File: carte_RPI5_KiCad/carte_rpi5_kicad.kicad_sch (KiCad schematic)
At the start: 30 parts, among them J1 Conn_01x03, J10 RPI5_40pins, J2 Conn_01x03, J3 Conn_01x03, J4 Conn_01x03, J5 Conn_01x03, J6 Conn_01x03, J7 Conn_01x03, J8 Conn_01x03, J9 XT60-M, SW1 SW_SPDT

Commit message: Mise à jour du PCB
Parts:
- F1: footprint Fuse:Fuse_0402_1005Metric -> librairie_empreintes:PTF-50
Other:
- note removed: "Demander à Thomas résistance sur interrupteur"
- note removed: "Rajouter des pins pour le moteur ; demander à Thomas pour les empreintes des pins"
- moved on the sheet: Conn_LPS22HB1, J10, R_SCL2, R_SDA2

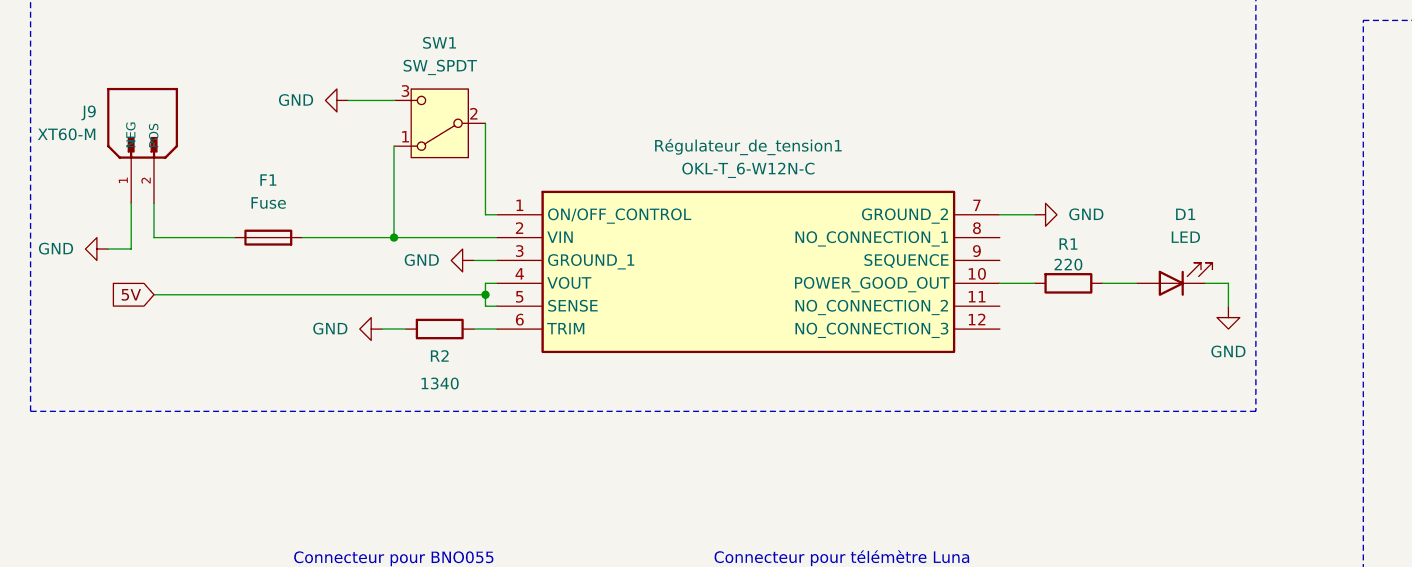
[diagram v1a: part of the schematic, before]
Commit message: changement_sens_connecteur_RPI
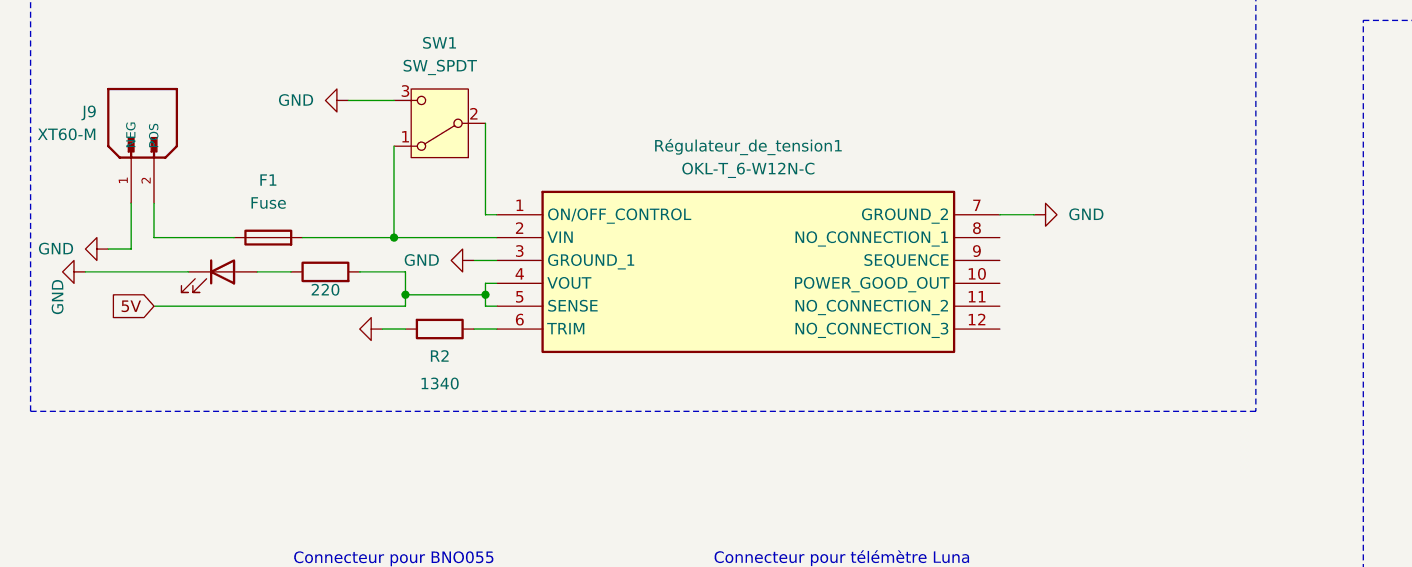
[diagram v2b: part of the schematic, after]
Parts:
- R1, R2, R_SCL2, R_SDA2: footprint Resistor_SMD:R_0805_2012Metric -> Resistor_SMD:R_1206_3216Metric_Pad1.30x1.75mm_HandSolder
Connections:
- net 5V: now also R1.2
- net at Régulateur_de_tension1.10 (POWER_GOOD_OUT): no longer R1.2
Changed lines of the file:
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@@
 	)
 	(junction
-		(at 66.04 49.53)
-		(diameter 0)
-		(color 0 0 0 0)
-	)
-	(junction
 		(at 345.44 218.44)
 		(diameter 0)
@@
 	)
 	(junction
+		(at 57.15 49.53)
+		(diameter 0)
+		(color 0 0 0 0)
+	)
+	(junction
 		(at 165.1 125.73)
 		(diameter 0)
@@
 	)
 	(junction
+		(at 66.04 49.53)
+		(diameter 0)
+		(color 0 0 0 0)
+	)
+	(junction
 		(at 247.65 39.37)
 		(diameter 0)
@@
 	(wire
 		(pts
+			(xy 66.04 49.53) (xy 66.04 50.8)
+		)
+		(stroke
+			(width 0)
+			(type default)
+		)
+	)
+	(wire
+		(pts
 			(xy 165.1 109.22) (xy 165.1 114.3)
 		)
@@
 	(wire
 		(pts
+			(xy 29.21 50.8) (xy 57.15 50.8)
+		)
+		(stroke
+			(width 0)
+			(type default)
+		)
+	)
+	(wire
+		(pts
 			(xy 66.04 48.26) (xy 66.04 49.53)
 		)
@@
 	(wire
 		(pts
-			(xy 123.19 48.26) (xy 127 48.26)
-		)
-		(stroke
-			(width 0)
-			(type default)
-		)
-	)
-	(wire
-		(pts
 			(xy 242.57 53.34) (xy 247.65 53.34)
 		)
@@
 	(wire
 		(pts
-			(xy 134.62 48.26) (xy 138.43 48.26)
-		)
-		(stroke
-			(width 0)
-			(type default)
-		)
-	)
-	(wire
-		(pts
 			(xy 63.5 156.21) (xy 63.5 161.29)
 		)
@@
 	(wire
 		(pts
-			(xy 148.59 48.26) (xy 148.59 50.8)
+			(xy 57.15 46.99) (xy 57.15 49.53)
 		)
 		(stroke
@@
 	(wire
 		(pts
-			(xy 198.12 143.51) (xy 205.74 143.51)
+			(xy 44.45 46.99) (xy 40.64 46.99)
 		)
 		(stroke
@@
 	(wire
 		(pts
-			(xy 186.69 72.39) (xy 186.69 73.66)
+			(xy 198.12 143.51) (xy 205.74 143.51)
 		)
 		(stroke
@@
 	(wire
 		(pts
-			(xy 176.53 151.13) (xy 185.42 151.13)
+			(xy 186.69 72.39) (xy 186.69 73.66)
 		)
 		(stroke
@@
 	(wire
 		(pts
-			(xy 203.2 120.65) (xy 205.74 120.65)
+			(xy 176.53 151.13) (xy 185.42 151.13)
 		)
 		(stroke
@@
 	(wire
 		(pts
-			(xy 55.88 43.18) (xy 67.31 43.18)
+			(xy 57.15 49.53) (xy 57.15 50.8)
 		)
 		(stroke
@@
 	(wire
 		(pts
-			(xy 55.88 33.02) (xy 55.88 43.18)
+			(xy 203.2 120.65) (xy 205.74 120.65)
 		)
 		(stroke
@@
 	(wire
 		(pts
-			(xy 146.05 48.26) (xy 148.59 48.26)
+			(xy 55.88 43.18) (xy 67.31 43.18)
 		)
 		(stroke
@@
 	(wire
 		(pts
-			(xy 29.21 49.53) (xy 66.04 49.53)
+			(xy 55.88 33.02) (xy 55.88 43.18)
 		)
 		(stroke
@@
 	(wire
 		(pts
+			(xy 33.02 46.99) (xy 21.59 46.99)
+		)
+		(stroke
+			(width 0)
+			(type default)
+		)
+	)
+	(wire
+		(pts
 			(xy 317.5 227.33) (xy 349.25 227.33)
 		)
@@
 	(wire
 		(pts
+			(xy 52.07 46.99) (xy 57.15 46.99)
+		)
+		(stroke
+			(width 0)
+			(type default)
+		)
+	)
+	(wire
+		(pts
 			(xy 242.57 50.8) (xy 247.65 50.8)
 		)
@@
 	(wire
 		(pts
-			(xy 66.04 49.53) (xy 66.04 50.8)
+			(xy 198.12 125.73) (xy 205.74 125.73)
 		)
 		(stroke
@@
 	(wire
 		(pts
-			(xy 198.12 125.73) (xy 205.74 125.73)
+			(xy 57.15 49.53) (xy 66.04 49.53)
 		)
 		(stroke
@@
 	(global_label "5V"
 		(shape input)
-		(at 29.21 49.53 180)
+		(at 29.21 50.8 180)
 		(fields_autoplaced yes)
 		(effects
@@
 		)
 		(property "Intersheetrefs" "${INTERSHEET_REFS}"
-			(at 23.9267 49.53 0)
+			(at 23.9267 50.8 0)
 			(effects
 				(font
@@
 	(symbol
 		(lib_id "Device:LED")
-		(at 142.24 48.26 180)
+		(at 36.83 46.99 0)
 		(unit 1)
 		(exclude_from_sim no)
@@
 		(fields_autoplaced yes)
 		(property "Reference" "D1"
-			(at 143.8275 40.64 0)
+			(at 35.2425 54.61 0)
 			(effects
 				(font
 					(size 1.27 1.27)
 				)
+				(hide yes)
 			)
 		)
 		(property "Value" "LED"
-			(at 143.8275 43.18 0)
+			(at 35.2425 52.07 0)
 			(effects
 				(font
 					(size 1.27 1.27)
 				)
+				(hide yes)
 			)
 		)
 		(property "Footprint" "LED_SMD:LED_0805_2012Metric"
-			(at 142.24 48.26 0)
+			(at 36.83 46.99 0)
 			(effects
 				(font
@@
 		)
 		(property "Datasheet" "~"
-			(at 142.24 48.26 0)
+			(at 36.83 46.99 0)
 			(effects
 				(font
@@
 		)
 		(property "Description" "Light emitting diode"
-			(at 142.24 48.26 0)
+			(at 36.83 46.99 0)
 			(effects
 				(font
@@
 		)
 		(property "Sim.Pins" "1=K 2=A"
-			(at 142.24 48.26 0)
+			(at 36.83 46.99 0)
 			(effects
 				(font
@@
 			)
 		)
-		(property "Footprint" "Resistor_SMD:R_0805_2012Metric"
+		(property "Footprint" "Resistor_SMD:R_1206_3216Metric_Pad1.30x1.75mm_HandSolder"
 			(at 60.96 51.562 90)
 			(effects
@@
 			)
 		)
-		(property "Footprint" "Resistor_SMD:R_0805_2012Metric"
+		(property "Footprint" "Resistor_SMD:R_1206_3216Metric_Pad1.30x1.75mm_HandSolder"
 			(at 163.322 118.11 90)
 			(effects
@@
 	(symbol
 		(lib_id "Device:R")
-		(at 130.81 48.26 270)
+		(at 48.26 46.99 90)
 		(unit 1)
 		(exclude_from_sim no)
@@
 		(dnp no)
 		(property "Reference" "R1"
-			(at 130.81 43.942 90)
+			(at 48.26 51.308 90)
 			(effects
 				(font
 					(size 1.27 1.27)
 				)
+				(hide yes)
 			)
 		)
 		(property "Value" "220"
-			(at 130.81 46.228 90)
+			(at 48.26 49.022 90)
 			(effects
 				(font
@@
 			)
 		)
-		(property "Footprint" "Resistor_SMD:R_0805_2012Metric"
-			(at 130.81 46.482 90)
+		(property "Footprint" "Resistor_SMD:R_1206_3216Metric_Pad1.30x1.75mm_HandSolder"
+			(at 48.26 48.768 90)
 			(effects
 				(font
@@
 		)
 		(property "Datasheet" "~"
-			(at 130.81 48.26 0)
+			(at 48.26 46.99 0)
 			(effects
 				(font
@@
 		)
 		(property "Description" "Resistor"
-			(at 130.81 48.26 0)
+			(at 48.26 46.99 0)
 			(effects
 				(font
@@
 			)
 		)
-		(property "Footprint" "Resistor_SMD:R_0805_2012Metric"
+		(property "Footprint" "Resistor_SMD:R_1206_3216Metric_Pad1.30x1.75mm_HandSolder"
 			(at 163.322 129.54 90)
 			(effects
@@
 				)
 				(justify right)
+				(hide yes)
 			)
 		)
@@
 	(symbol
 		(lib_id "power:GND")
-		(at 148.59 50.8 0)
+		(at 21.59 46.99 270)
 		(unit 1)
 		(exclude_from_sim no)
@@
 		(on_board yes)
 		(dnp no)
-		(fields_autoplaced yes)
 		(property "Reference" "#PWR05"
-			(at 148.59 57.15 0)
+			(at 15.24 46.99 0)
 			(effects
 				(font
@@
 		)
 		(property "Value" "GND"
-			(at 148.59 55.88 0)
+			(at 18.542 49.784 0)
 			(effects
 				(font
@@
 		)
 		(property "Footprint" ""
-			(at 148.59 50.8 0)
+			(at 21.59 46.99 0)
 			(effects
 				(font
@@
 		)
 		(property "Datasheet" ""
-			(at 148.59 50.8 0)
+			(at 21.59 46.99 0)
 			(effects
 				(font
@@
 		)
 		(property "Description" "Power symbol creates a global label with name \"GND\" , ground"
-			(at 148.59 50.8 0)
+			(at 21.59 46.99 0)
 			(effects
 				(font

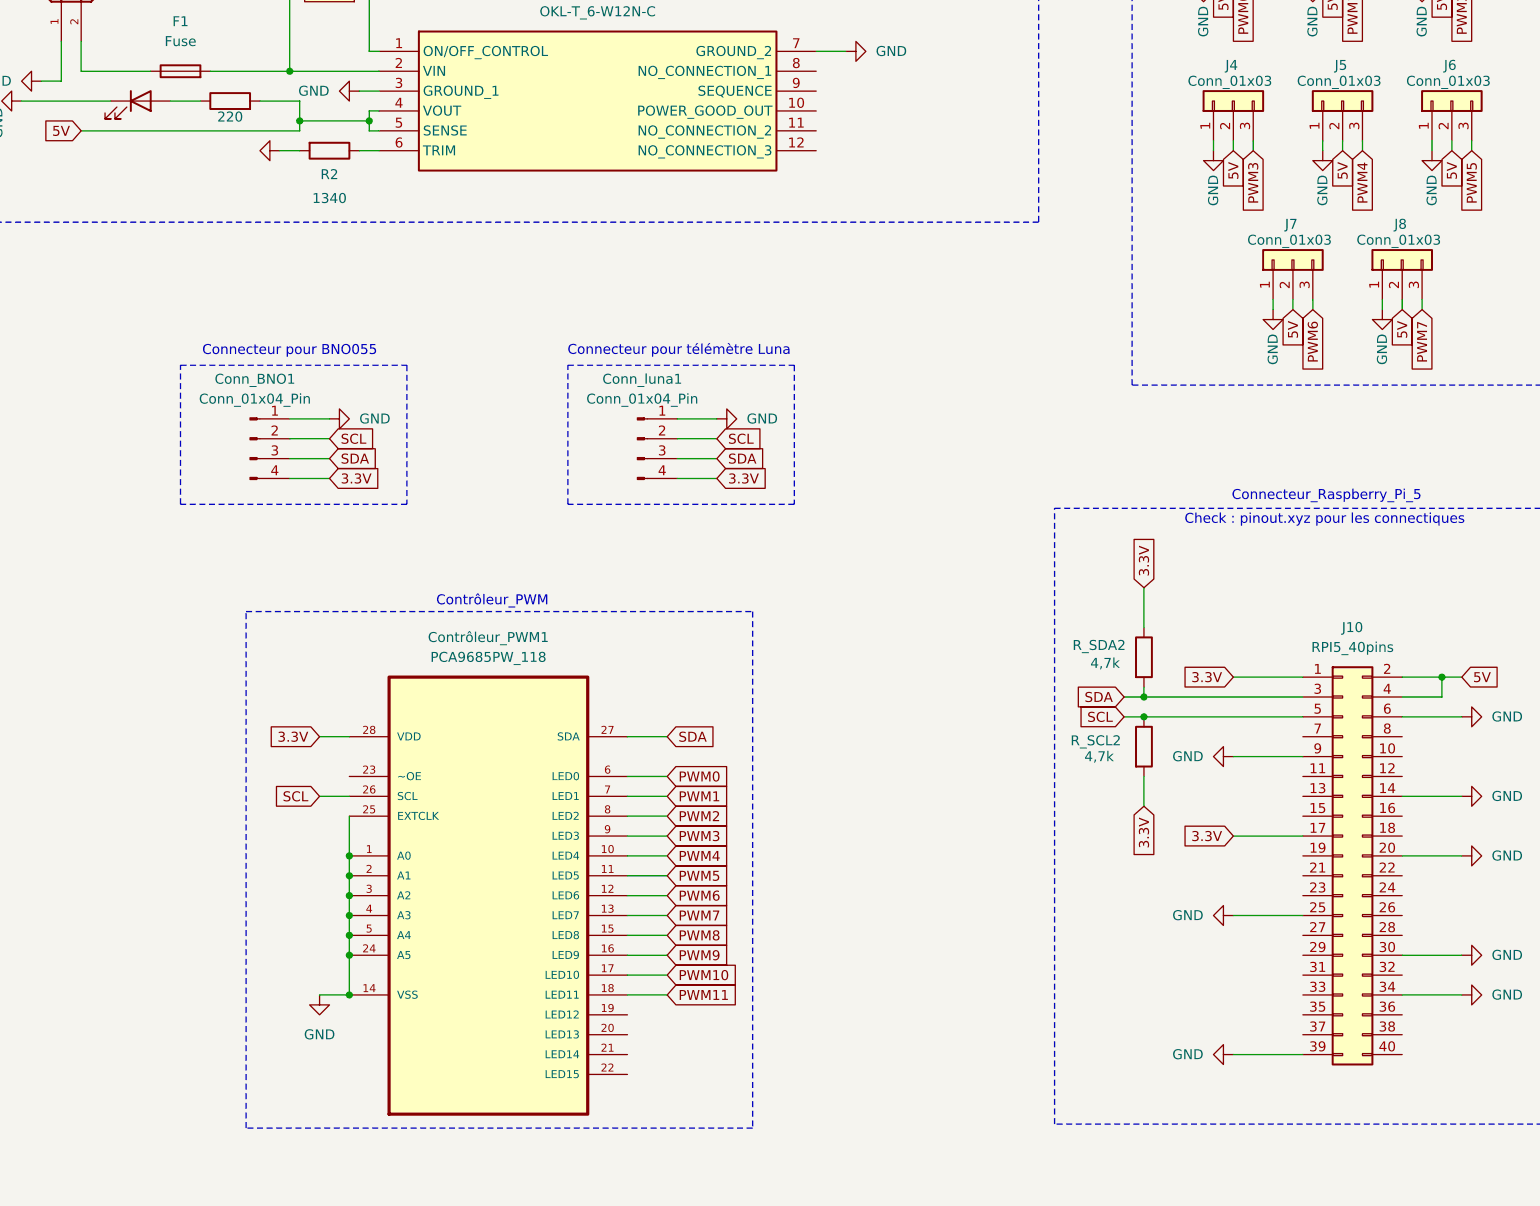
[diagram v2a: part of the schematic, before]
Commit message: modif_PCB_ajout_resistance
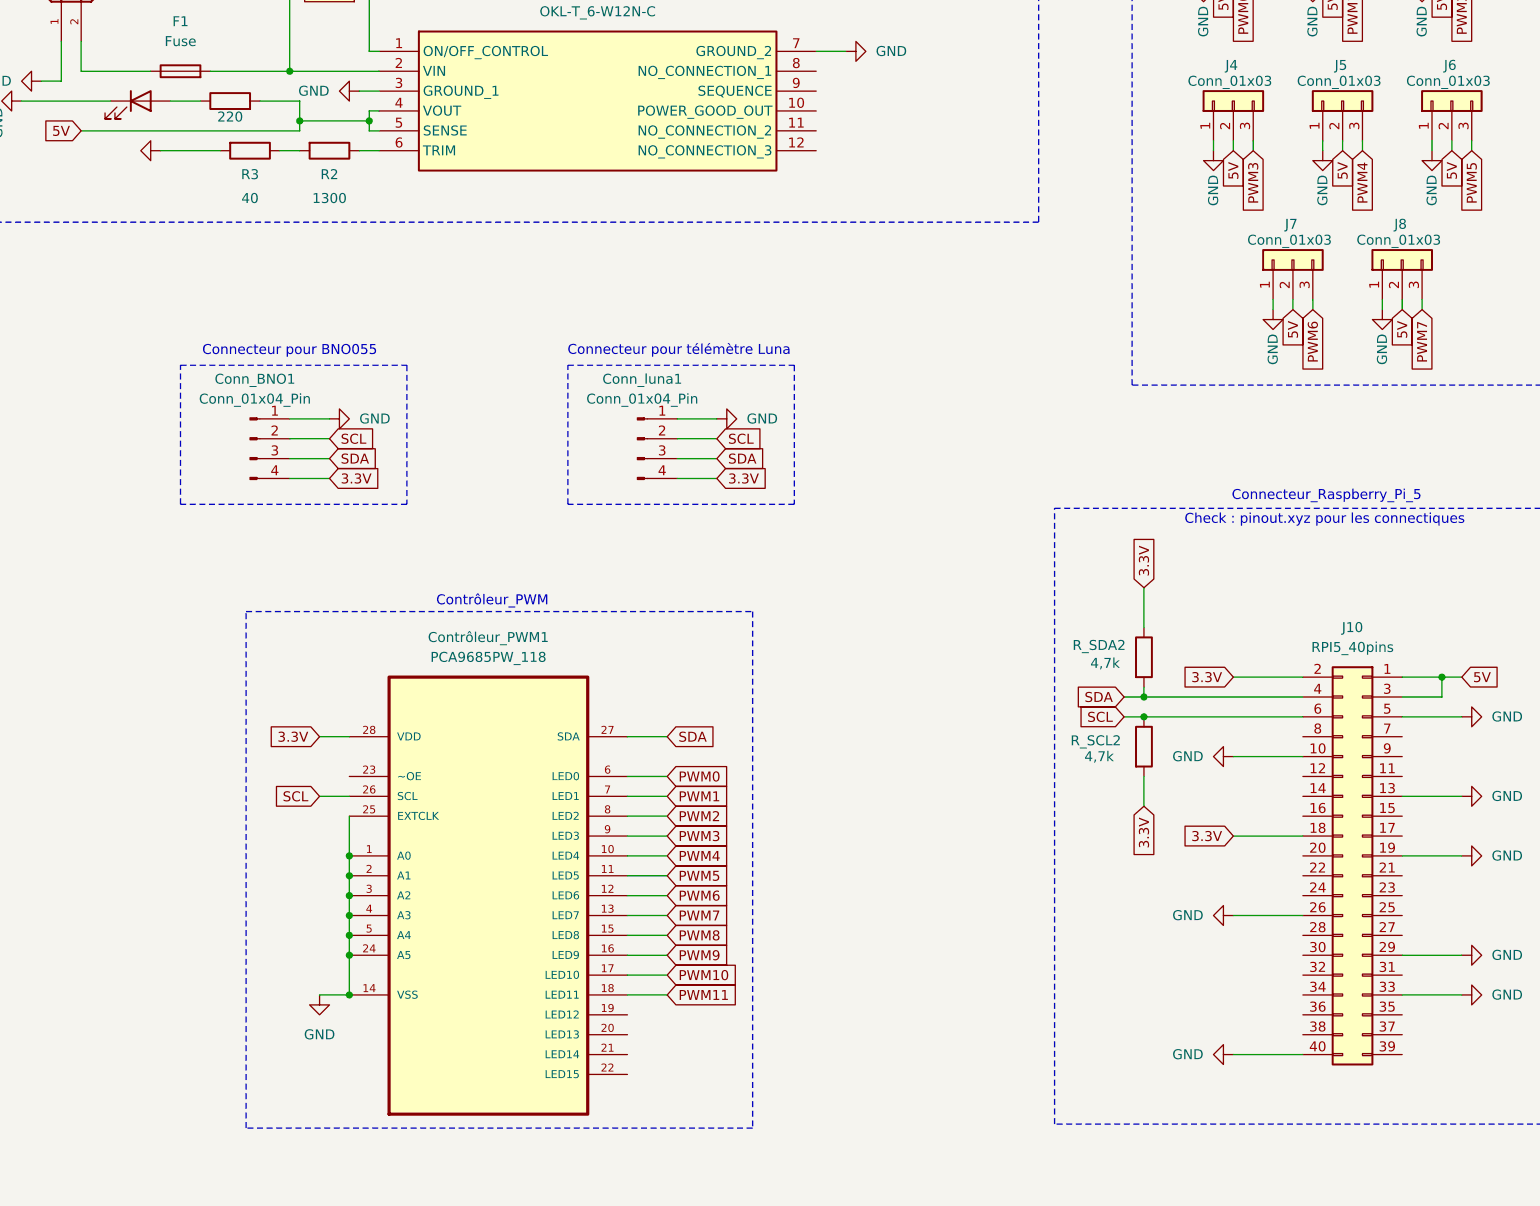
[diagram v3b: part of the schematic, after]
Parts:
- added R3: 40, Resistor_SMD:R_1206_3216Metric_Pad1.30x1.75mm_HandSolder, symbol Device:R
- R2: value 1340 -> 1300
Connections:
- net 3.3V: now also J10.18 (Pin_18), J10.2 (Pin_2); no longer J10.1 (Pin_1), J10.17 (Pin_17)
- net 5V: now also J10.1 (Pin_1), J10.3 (Pin_3); no longer J10.2 (Pin_2), J10.4 (Pin_4)
- net GND: now also J10.10 (Pin_10), J10.13 (Pin_13), J10.19 (Pin_19), J10.26 (Pin_26), J10.29 (Pin_29), J10.33 (Pin_33), J10.40 (Pin_40), J10.5 (Pin_5), R3.2; no longer J10.14 (Pin_14), J10.20 (Pin_20), J10.25 (Pin_25), J10.30 (Pin_30), J10.34 (Pin_34), J10.39 (Pin_39), J10.6 (Pin_6), J10.9 (Pin_9), R2.2
- net SCL: now also J10.6 (Pin_6); no longer J10.5 (Pin_5)
- net SDA: now also J10.4 (Pin_4); no longer J10.3 (Pin_3)
- new net: R2.2, R3.1
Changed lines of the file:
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@@
 	(wire
 		(pts
+			(xy 54.61 53.34) (xy 57.15 53.34)
+		)
+		(stroke
+			(width 0)
+			(type default)
+		)
+	)
+	(wire
+		(pts
 			(xy 123.19 40.64) (xy 127 40.64)
 		)
@@
 	(wire
 		(pts
+			(xy 39.37 53.34) (xy 46.99 53.34)
+		)
+		(stroke
+			(width 0)
+			(type default)
+		)
+	)
+	(wire
+		(pts
 			(xy 165.1 133.35) (xy 165.1 137.16)
 		)
@@
 	(wire
 		(pts
-			(xy 54.61 53.34) (xy 57.15 53.34)
-		)
-		(stroke
-			(width 0)
-			(type default)
-		)
-	)
-	(wire
-		(pts
 			(xy 337.82 26.67) (xy 344.17 26.67)
 		)
@@
 	)
 	(symbol
+		(lib_id "Device:R")
+		(at 50.8 53.34 270)
+		(unit 1)
+		(exclude_from_sim no)
+		(in_bom yes)
+		(on_board yes)
+		(dnp no)
+		(property "Reference" "R3"
+			(at 50.8 56.388 90)
+			(effects
+				(font
+					(size 1.27 1.27)
+				)
+			)
+		)
+		(property "Value" "40"
+			(at 50.8 59.436 90)
+			(effects
+				(font
+					(size 1.27 1.27)
+				)
+			)
+		)
+		(property "Footprint" "Resistor_SMD:R_1206_3216Metric_Pad1.30x1.75mm_HandSolder"
+			(at 50.8 51.562 90)
+			(effects
+				(font
+					(size 1.27 1.27)
+				)
+				(hide yes)
+			)
+		)
+		(property "Datasheet" "~"
+			(at 50.8 53.34 0)
+			(effects
+				(font
+					(size 1.27 1.27)
+				)
+				(hide yes)
+			)
+		)
+		(property "Description" "Resistor"
+			(at 50.8 53.34 0)
+			(effects
+				(font
+					(size 1.27 1.27)
+				)
+				(hide yes)
+			)
+		)
+		(pin "1"
+		)
+		(pin "2"
+		)
+		(instances
+			(project "carte_rpi5_kicad"
+				(path "/1781f24e-6d21-4940-8f28-5db05927caba"
+					(reference "R3")
+					(unit 1)
+				)
+			)
+		)
+	)
+	(symbol
 		(lib_id "power:GND")
 		(at 205.74 125.73 90)
@@
 			)
 		)
-		(property "Value" "1340"
+		(property "Value" "1300"
 			(at 60.96 59.436 90)
 			(effects
@@
 	(symbol
 		(lib_id "Connector_Generic:Conn_02x20_Odd_Even")
-		(at 190.5 143.51 0)
+		(at 193.04 143.51 0)
+		(mirror y)
 		(unit 1)
 		(exclude_from_sim no)
@@
 		)
 		(property "Footprint" "Connector_PinSocket_2.54mm:PinSocket_2x20_P2.54mm_Vertical"
-			(at 190.5 143.51 0)
+			(at 193.04 143.51 0)
 			(effects
 				(font
@@
 		)
 		(property "Datasheet" "~"
-			(at 190.5 143.51 0)
+			(at 193.04 143.51 0)
 			(effects
 				(font
@@
 		)
 		(property "Description" "Generic connector, double row, 02x20, odd/even pin numbering scheme (row 1 odd numbers, row 2 even numbers), script generated (kicad-library-utils/schlib/autogen/connector/)"
-			(at 190.5 143.51 0)
+			(at 193.04 143.51 0)
 			(effects
 				(font
@@
 	(symbol
 		(lib_id "power:GND")
-		(at 54.61 53.34 270)
+		(at 39.37 53.34 270)
 		(unit 1)
 		(exclude_from_sim no)
@@
 		(fields_autoplaced yes)
 		(property "Reference" "#PWR03"
-			(at 48.26 53.34 0)
+			(at 33.02 53.34 0)
 			(effects
 				(font
@@
 		)
 		(property "Value" "GND"
-			(at 50.8 53.3399 90)
+			(at 35.56 53.3399 90)
 			(effects
 				(font
@@
 		)
 		(property "Footprint" ""
-			(at 54.61 53.34 0)
+			(at 39.37 53.34 0)
 			(effects
 				(font
@@
 		)
 		(property "Datasheet" ""
-			(at 54.61 53.34 0)
+			(at 39.37 53.34 0)
 			(effects
 				(font
@@
 		)
 		(property "Description" "Power symbol creates a global label with name \"GND\" , ground"
-			(at 54.61 53.34 0)
+			(at 39.37 53.34 0)
 			(effects
 				(font
